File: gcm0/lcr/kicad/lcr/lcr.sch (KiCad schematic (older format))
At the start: 70 parts

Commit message: 显示上臂下臂实部虚部1
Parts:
- removed U?: CD4053B, symbol Analog_Switch:CD4053B
- added U?: CD4053B, symbol yjmwxwx:CD4053B
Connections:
- net +5V: now also U?.16 (VDD)
- net -5V: now also U?.7 (VEE)
- net GND: now also U?.6 (INH), U?.8 (VSS)
- net at U?.3 (+): now also U?.15 (b)
- net at U?.12 (+): now also U?.4 (c)
- net at R?.2, U?.1: now also U?.1 (by)
- net at Q?.1 (C), R?.2: now also U?.10 (B), U?.11 (A), U?.9 (C)
- net at R?.1, R?.2: now also U?.2 (bx)
- net at D?.1 (K), D?.2 (A), R?.1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: now also U?.3 (cy)
- net at D?.1 (K), D?.2 (A), R?.1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: now also U?.5 (cx)
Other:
- moved on the sheet: C?, Q?, R?, U?, U?A, U?B, U?C, U?D, U?E, Y?

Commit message: 加入量程切换
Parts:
- removed R?: R, symbol Device:R
- added R24: 100, symbol Device:R
- added R25, R4, R5 (x2): 1K, symbol Device:R
- added R26: 10K, symbol Device:R
- added R27: 100K, symbol Device:R
- added U?: CD4052B, symbol Analog_Switch:CD4052B
- BT1, BT2: renamed from BT?; value Battery_Cell -> 9V
- C1, C11, C12, C2, C4: renamed from C?; value CP -> 100UF
- C10, C3, C7, C9: renamed from C?; value C -> 104
- C5, C6: renamed from C?; value C -> 22PF
- C8: renamed from C?; value C -> 103
- D1, D2, D3, D4: renamed from D?; value D -> 1N4007
- R1, R13, R2, R3, R9: renamed from R?; value R -> 1K
- R10, R11, R12, R7, R8: renamed from R?; value R -> 100
- R14, R15, R16, R17, R18, R19: renamed from R?; value R -> 22K
- R20, R21: renamed from R?; value R -> 100K
- R22, R23: renamed from R?; value R -> 510
- R6: renamed from R?; value R -> 10K
- RV1: renamed from RV?; value R_POT_TRIM -> 10K
- Y1: renamed from Y?; value Crystal -> 8M
- gave numbers to parts that had none: 5
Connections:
- net +5V: now also U?.16 (VDD)
- net -5V: now also U?.6 (INH)
- net GND: now also U?.7 (VEE), U?.8 (VSS)
- net RCLK: now also R5.2; no longer Q?.2 (B)
- net SER: now also R4.2; no longer Q1.2 (B)
- net SRCLK: now also R5.2; no longer Q2.2 (B)
- net at D?.1 (K), D?.2 (A), R11.2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: now also D?.1 (K), D?.2 (A), R11.1, U?.5 (cx), Z.2, R24.1, R25.1, R26.1, R27.1
- net at U?.1 (by): now also U?.3 (Y); no longer U?.1
- net at R10.2, U?.2 (bx), Z.1: now also R10.1, R8.2
- net liangchengkaiguan1: now reaches U?.6 (QG)
- net liangchengkaiguan1: now also U?.10 (A)
- net liangchengkaiguan: now reaches U?.7 (QH)
- net liangchengkaiguan: now also U?.9 (B)
- new net: R27.2, U?.1 (Y0), U?.12 (X0)
- new net: R24.2, U?.11 (X3), U?.4 (Y3)
- new net: U?.1, U?.13 (X)
- new net: R26.2, U?.14 (X1), U?.5 (Y1)
- new net: R25.2, U?.15 (X2), U?.2 (Y2)
- new net: Q?.2 (B), R5.1
- new net: Q2.2 (B), R5.1
- new net: Q1.2 (B), R4.1
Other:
- moved on the sheet: C5, C6, C7, R6, U?, Y1, Z

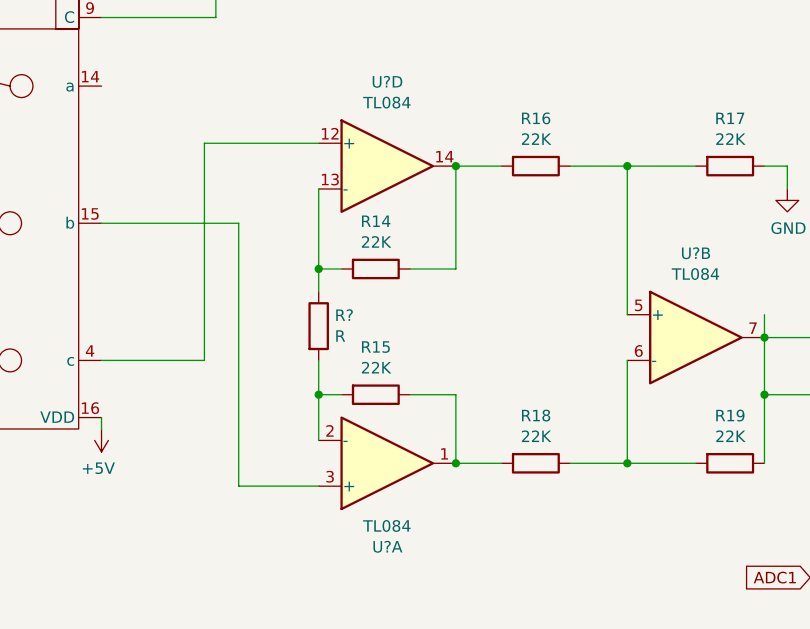
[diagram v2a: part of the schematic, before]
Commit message: 检波改成DFT计算
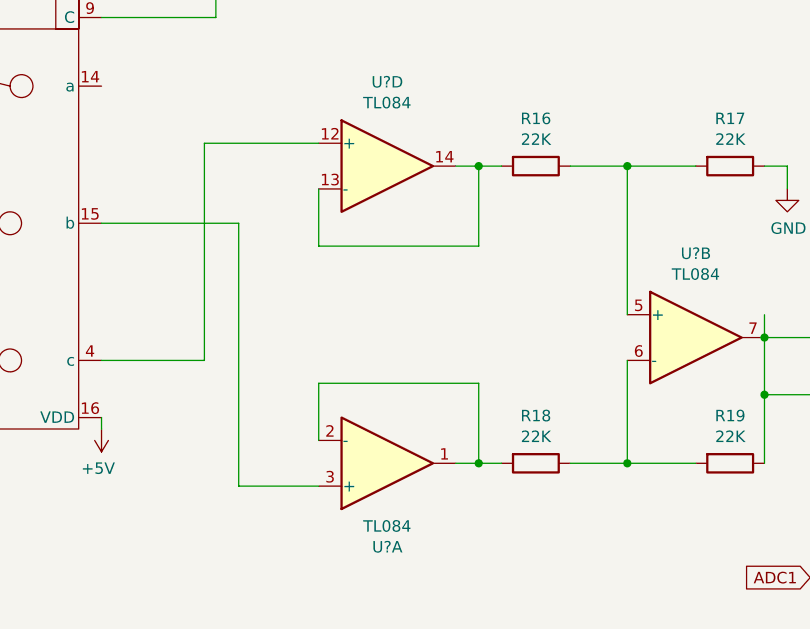
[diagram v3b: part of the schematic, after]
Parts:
- removed R14, R15: 22K, symbol Device:R
- removed R?: R, symbol Device:R
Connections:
- net at R18.2, U?.1: now also U?.2 (-)
- net at U?.13 (-): now also R16.2, U?.14
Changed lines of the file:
@@
 Wire Wire Line
 	7950 4550 8200 4550
-Connection ~ 7450 4550
-Wire Wire Line
-	7650 4550 7450 4550
+Wire Wire Line
+	7650 4550 7550 4550
 Wire Wire Line
 	7950 3250 8200 3250
-Connection ~ 7450 3250
-Wire Wire Line
-	7650 3250 7450 3250
-Connection ~ 6850 3700
-Wire Wire Line
-	6850 3800 6850 3700
-Connection ~ 6850 4250
-Wire Wire Line
-	6850 4100 6850 4250
-Wire Wire Line
-	7450 4250 7450 4550
-Wire Wire Line
-	7250 4250 7450 4250
-Wire Wire Line
-	6850 4250 6950 4250
-Wire Wire Line
-	6850 4450 6850 4250
-Wire Wire Line
-	7450 3700 7450 3250
-Wire Wire Line
-	7250 3700 7450 3700
-Wire Wire Line
-	6850 3700 6850 3350
-Wire Wire Line
-	6950 3700 6850 3700
-$Comp
-L Device:R R?
-U 1 1 5D601C03
-P 6850 3950
-F 0 "R?" H 6920 3996 50  0000 L CNN
-F 1 "R" H 6920 3905 50  0000 L CNN
-F 2 "" V 6780 3950 50  0001 C CNN
-F 3 "~" H 6850 3950 50  0001 C CNN
-	1    6850 3950
-	1    0    0    -1
-$EndComp
-$Comp
-L Device:R R15
-U 1 1 5D60073B
-P 7100 4250
-F 0 "R15" V 6893 4250 50  0000 C CNN
-F 1 "22K" V 6984 4250 50  0000 C CNN
-F 2 "" V 7030 4250 50  0001 C CNN
-F 3 "~" H 7100 4250 50  0001 C CNN
-	1    7100 4250
-	0    1    1    0
-$EndComp
-$Comp
-L Device:R R14
-U 1 1 5D5FADB2
-P 7100 3700
-F 0 "R14" V 6893 3700 50  0000 C CNN
-F 1 "22K" V 6984 3700 50  0000 C CNN
-F 2 "" V 7030 3700 50  0001 C CNN
-F 3 "~" H 7100 3700 50  0001 C CNN
-	1    7100 3700
-	0    1    1    0
-$EndComp
+Wire Wire Line
+	7650 3250 7550 3250
 $Comp
 L Device:R R19
@@
 Wire Notes Line
 	11150 9800 11150 7300
+Wire Wire Line
+	6850 4450 6850 4200
+Wire Wire Line
+	6850 4200 7550 4200
+Wire Wire Line
+	7550 4200 7550 4550
+Connection ~ 7550 4550
+Wire Wire Line
+	7550 4550 7450 4550
+Wire Wire Line
+	6850 3350 6850 3600
+Wire Wire Line
+	6850 3600 7550 3600
+Wire Wire Line
+	7550 3600 7550 3250
+Connection ~ 7550 3250
+Wire Wire Line
+	7550 3250 7450 3250
 $EndSCHEMATC

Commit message: 加入滤波器1
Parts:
- C10, C9: value 104 -> 103
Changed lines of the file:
@@
 P 10250 5050
 F 0 "C9" V 9998 5050 50  0000 C CNN
-F 1 "104" V 10089 5050 50  0000 C CNN
+F 1 "103" V 10089 5050 50  0000 C CNN
 F 2 "" H 10288 4900 50  0001 C CNN
 F 3 "~" H 10250 5050 50  0001 C CNN
@@
 P 9750 5050
 F 0 "C10" V 9498 5050 50  0000 C CNN
-F 1 "104" V 9589 5050 50  0000 C CNN
+F 1 "103" V 9589 5050 50  0000 C CNN
 F 2 "" H 9788 4900 50  0001 C CNN
 F 3 "~" H 9750 5050 50  0001 C CNN

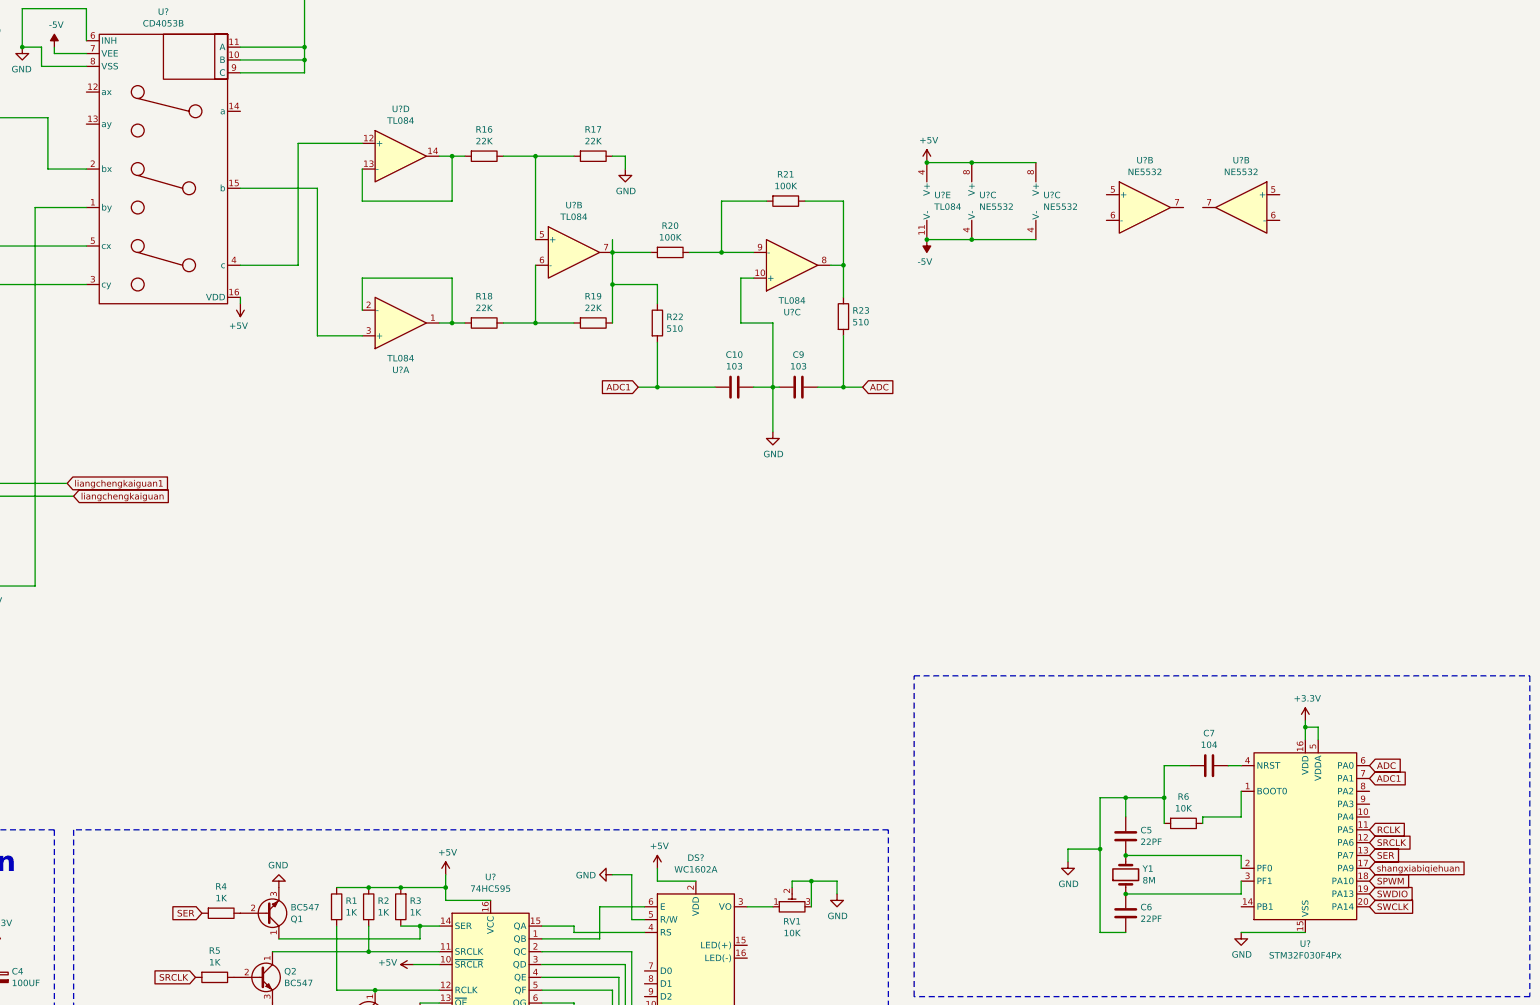
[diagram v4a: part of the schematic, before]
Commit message: 加入放大电路
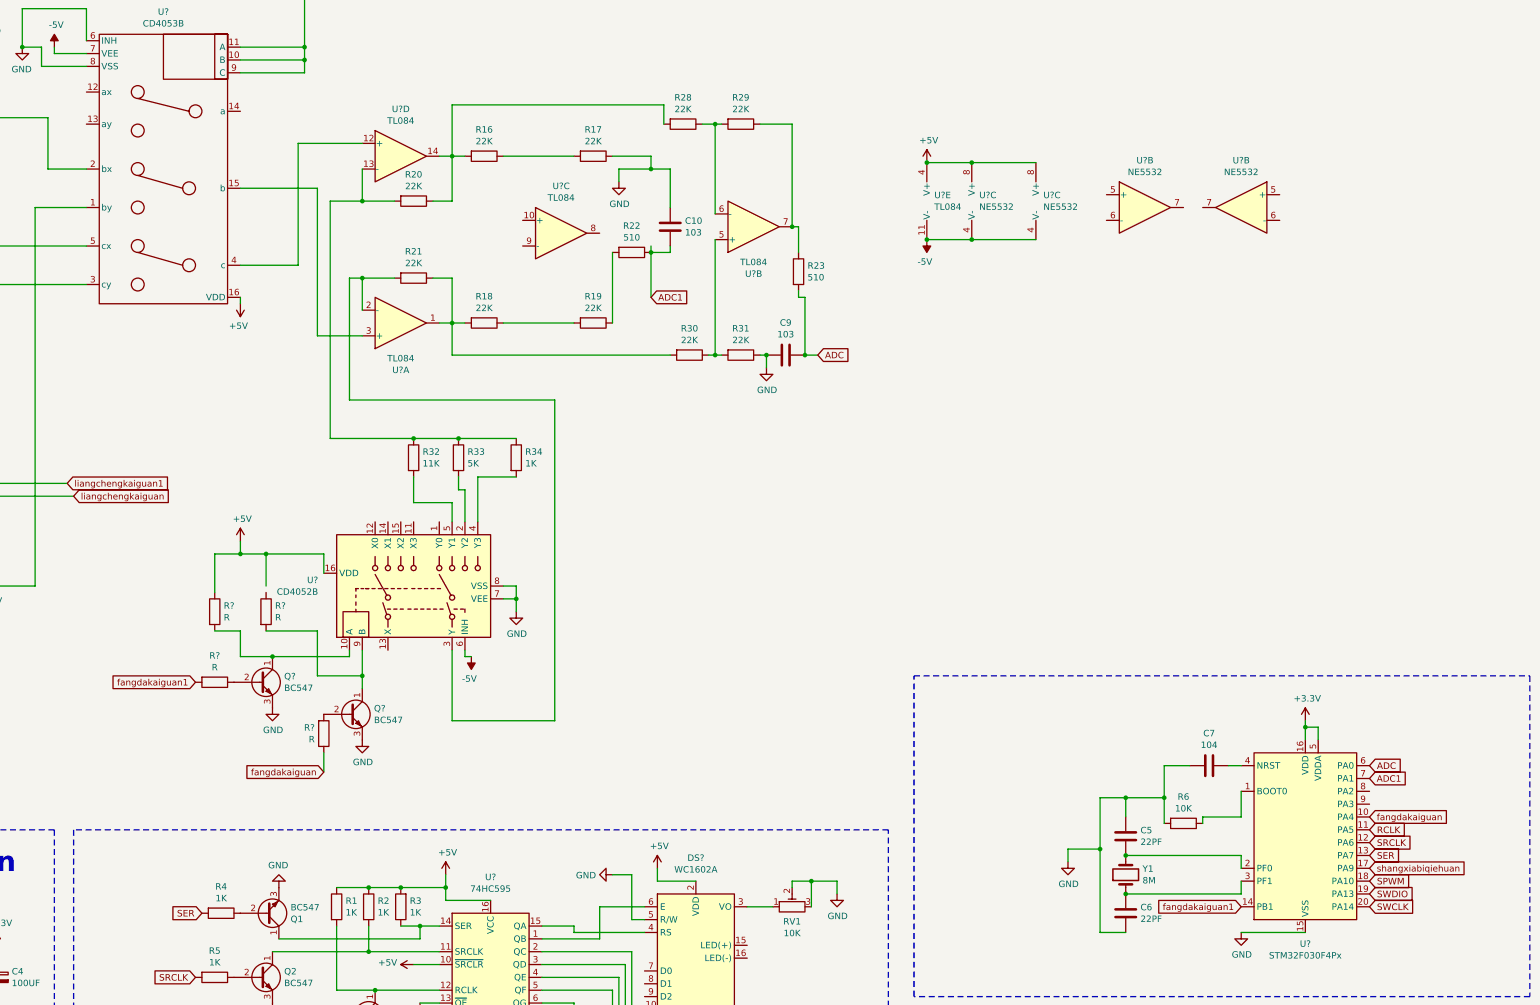
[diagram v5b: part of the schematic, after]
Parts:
- removed U?: TL084, symbol Amplifier_Operational:TL084
- added Q? (x2): BC547, Package_TO_SOT_THT:TO-92_Inline, symbol Transistor_BJT:BC547
- added R28, R29, R30, R31: 22K, symbol Device:R
- added R32: 11K, symbol Device:R
- added R33: 5K, symbol Device:R
- added R34: 1K, symbol Device:R
- added R? (x4): R, symbol Device:R
- added U?: CD4052B, symbol Analog_Switch:CD4052B
- added U?: TL084, symbol Amplifier_Operational:TL084
- R20, R21: value 100K -> 22K
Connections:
- net +5V: now also R?.1, U?.16 (VDD)
- net -5V: now also U?.6 (INH)
- net ADC1: now also R22.1; no longer R22.2
- net GND: now also Q?.3 (E), Q?.3 (E), R31.1, U?.7 (VEE), U?.8 (VSS); no longer U?.10 (+)
- net fangdakaiguan: now reaches U?.10 (PA4)
- net fangdakaiguan: now also R?.1
- net fangdakaiguan1: now reaches U?.14 (PB1)
- net fangdakaiguan1: now also R?.2
- net at R18.2, U?.1: now also R21.1, R30.2; no longer U?.2 (-)
- net at R16.2, U?.14: now also R20.1, R28.2; no longer U?.13 (-)
- new net: R21.2, U?.2 (-), U?.3 (Y)
- new net: R20.2, R32.1, R33.1, R34.1, U?.13 (-)
- new net: R19.1, R22.2
- new net: R23.1, R29.1, U?.7
- new net: Q?.1 (C), R?.2, U?.10 (A)
- new net: R33.2, U?.2 (Y2)
- new net: R34.2, U?.4 (Y3)
- new net: R32.2, U?.5 (Y1)
- new net: Q?.1 (C), R?.2, U?.9 (B)
- new net: Q?.2 (B), R?.1
- new net: Q?.2 (B), R?.2
- new net: R30.1, R31.2, U?.5 (+)
- new net: R28.1, R29.2, U?.6 (-)
- now unconnected: U?.8, U?.9 (-)
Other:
- moved on the sheet: C9, R23, U?C

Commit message: 修改自动量程
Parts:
- removed U?: CD4052B, symbol Analog_Switch:CD4052B
- added R35: 100k, symbol Device:R
- added SW1, SW2: SW_Push, symbol Switch:SW_Push
- added U?: CD4052B, symbol Analog_Switch:CD4052B
- R20, R21: value 22K -> 100k
- R32: value 11K -> 50k
- R33: value 5K -> 10k
- R34: value 1K -> 5k
- R36, R37, R38, R39: renamed from R?; value R -> 1k
- U5: renamed from U?; value STM32F030F4Px -> STM32F030F4P6
- gave numbers to parts that had none: 11
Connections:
- net +5V: now also R37.1, U?.16 (VDD)
- net -5V: now also U7.7 (VEE), U?.7 (VEE); no longer U7.6 (INH)
- net GND: now also U7.6 (INH), SW1.2, SW2.2, U?.6 (INH), U?.8 (VSS); no longer U7.7 (VEE)
- net liangchengkaiguan: now also U?.9 (B)
- net liangchengkaiguan1: now also U?.10 (A)
- net at U5.8 (PA2): now also SW1.1
- net at U5.9 (PA3): now also SW2.1
- net at U10.10 (+): now also R16.1, R17.2
- net at U10.8: now also R19.1, R22.2
- net at U10.9 (-): now also R18.1, R19.2
- net at R20.2, R32.1, R33.1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: now also R35.1
- net at U11.1 (by): now also U?.3 (Y)
- net at R27.2: now also U?.1 (Y0), U?.12 (X0)
- net at R24.2: now also U?.11 (X3), U?.4 (Y3)
- net at U8.1: now also U?.13 (X)
- net at R26.2: now also U?.14 (X1), U?.5 (Y1)
- net at R25.2: now also U?.15 (X2), U?.2 (Y2)
- net at U7.1 (Y0): now also R35.2

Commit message: 修改放大电路
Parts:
- removed C10: 103, symbol Device:C
- removed R16, R17: 22K, symbol Device:R
- removed R32: 50k, symbol Device:R
- removed R33: 10k, symbol Device:R
- removed R34: 5k, symbol Device:R
- removed R35: 100k, symbol Device:R
- added R24: 2K, symbol Device:R
- added R25, R26: 1K, symbol Device:R
- added R27: 29K, symbol Device:R
- added U10: NE5532, symbol Amplifier_Operational:NE5532
- C9: value 103 -> 102
- R17: renamed from R12; value 100 -> 1k
- R18, R19: value 22K -> 22k
- R20, R21: value 100k -> 22k
- R22: value 510 -> 22K
- R23: value 510 -> 5K
- R28, R29: value 22K -> 100k
- R30, R31: value 22K -> 510
- renumbered R7 to R11, R11 to R12, R24 to R13, R25 to R14, R26 to R15, R27 to R16, R36 to R32, R37 to R33, R38 to R34, R39 to R35, R5 to R6, R6 to R7
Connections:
- net +5V: now also U10.8 (V+)
- net -5V: now also U10.4 (V-)
- net ADC: now also R31.1; no longer C9.1, R23.2
- net ADC1: now also R30.1; no longer R22.1
- net GND: now also R19.1, R25.1, R26.2, U10.5 (+); no longer R31.1
- net at U10.10 (+): now also R18.1, R19.2
- net at R20.2: now also U10.1, U10.2 (-); no longer U10.13 (-)
- net at U7.11 (X3): now also R21.1, R22.1, U10.8
- net at U7.12 (X0): now also R24.2, R25.2
- net at U7.13 (X): now also U10.5 (+)
- net at U7.14 (X1): now also R23.2, R24.1
- net at U7.15 (X2): now also R22.2, R23.1
- new net: R20.1, R21.2, U10.9 (-)
- new net: R18.2, U10.13 (-), U10.14
- new net: R26.1, R27.2, U10.6 (-)
- new net: C9.1, R27.1, R28.1, U10.3 (+), U10.7
- new net: R30.2, U10.1, U10.2 (-)
- new net: R28.2, R29.2, U10.6 (-)
- new net: R29.1, R31.2, U10.7
- now unconnected: U7.3 (Y)
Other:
- note added: "mcu"
- moved on the sheet: Q4, Q5, R32, R33, R34, R35, U10A, U10B, U10D, U10E, U7, U8B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

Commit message: 修改除法
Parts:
- added R36: 1k, symbol Device:R
- R8: value 100 -> 200
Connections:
- net at C9.1, R28.1, U10.3 (+): now also R36.2; no longer R27.1, U10.7
- new net: R27.1, R36.1, U10.7
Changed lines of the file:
@@
 P 1650 1800
 F 0 "R8" V 1443 1800 50  0000 C CNN
-F 1 "100" V 1534 1800 50  0000 C CNN
+F 1 "200" V 1534 1800 50  0000 C CNN
 F 2 "" V 1580 1800 50  0001 C CNN
 F 3 "~" H 1650 1800 50  0001 C CNN
@@
 $EndComp
 Wire Wire Line
-	12550 4450 12550 4250
-Wire Wire Line
-	12550 3950 12200 3950
-Connection ~ 12200 3950
-Wire Wire Line
-	12900 4000 12550 4000
-Connection ~ 12550 4000
-Wire Wire Line
-	12550 4000 12550 3950
-Wire Wire Line
 	12550 4750 12550 5300
 Wire Wire Line
@@
 $EndComp
 Wire Wire Line
-	12100 4750 12100 4250
-Wire Wire Line
-	12100 4250 12550 4250
-Connection ~ 12550 4250
-Wire Wire Line
-	12550 4250 12550 4000
-Wire Wire Line
 	12100 5050 12100 5500
 Wire Wire Line
@@
 Wire Wire Line
 	12800 4850 12800 5300
+$Comp
+L Device:R R36
+U 1 1 5D7E3B98
+P 12200 4100
+F 0 "R36" H 12270 4146 50  0000 L CNN
+F 1 "1k" H 12270 4055 50  0000 L CNN
+F 2 "" V 12130 4100 50  0001 C CNN
+F 3 "~" H 12200 4100 50  0001 C CNN
+	1    12200 4100
+	1    0    0    -1
+$EndComp
+Connection ~ 12200 3950
+Wire Wire Line
+	12100 4750 12100 4250
+Wire Wire Line
+	12100 4250 12200 4250
+Wire Wire Line
+	12200 4250 12550 4250
+Connection ~ 12200 4250
+Wire Wire Line
+	12550 4250 12550 4450
+Wire Wire Line
+	12900 4000 12550 4000
+Wire Wire Line
+	12550 4000 12550 4250
+Connection ~ 12550 4250
 $EndSCHEMATC
